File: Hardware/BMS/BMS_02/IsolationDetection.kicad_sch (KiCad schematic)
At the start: 11 parts, among them U23 OPA320-Q1

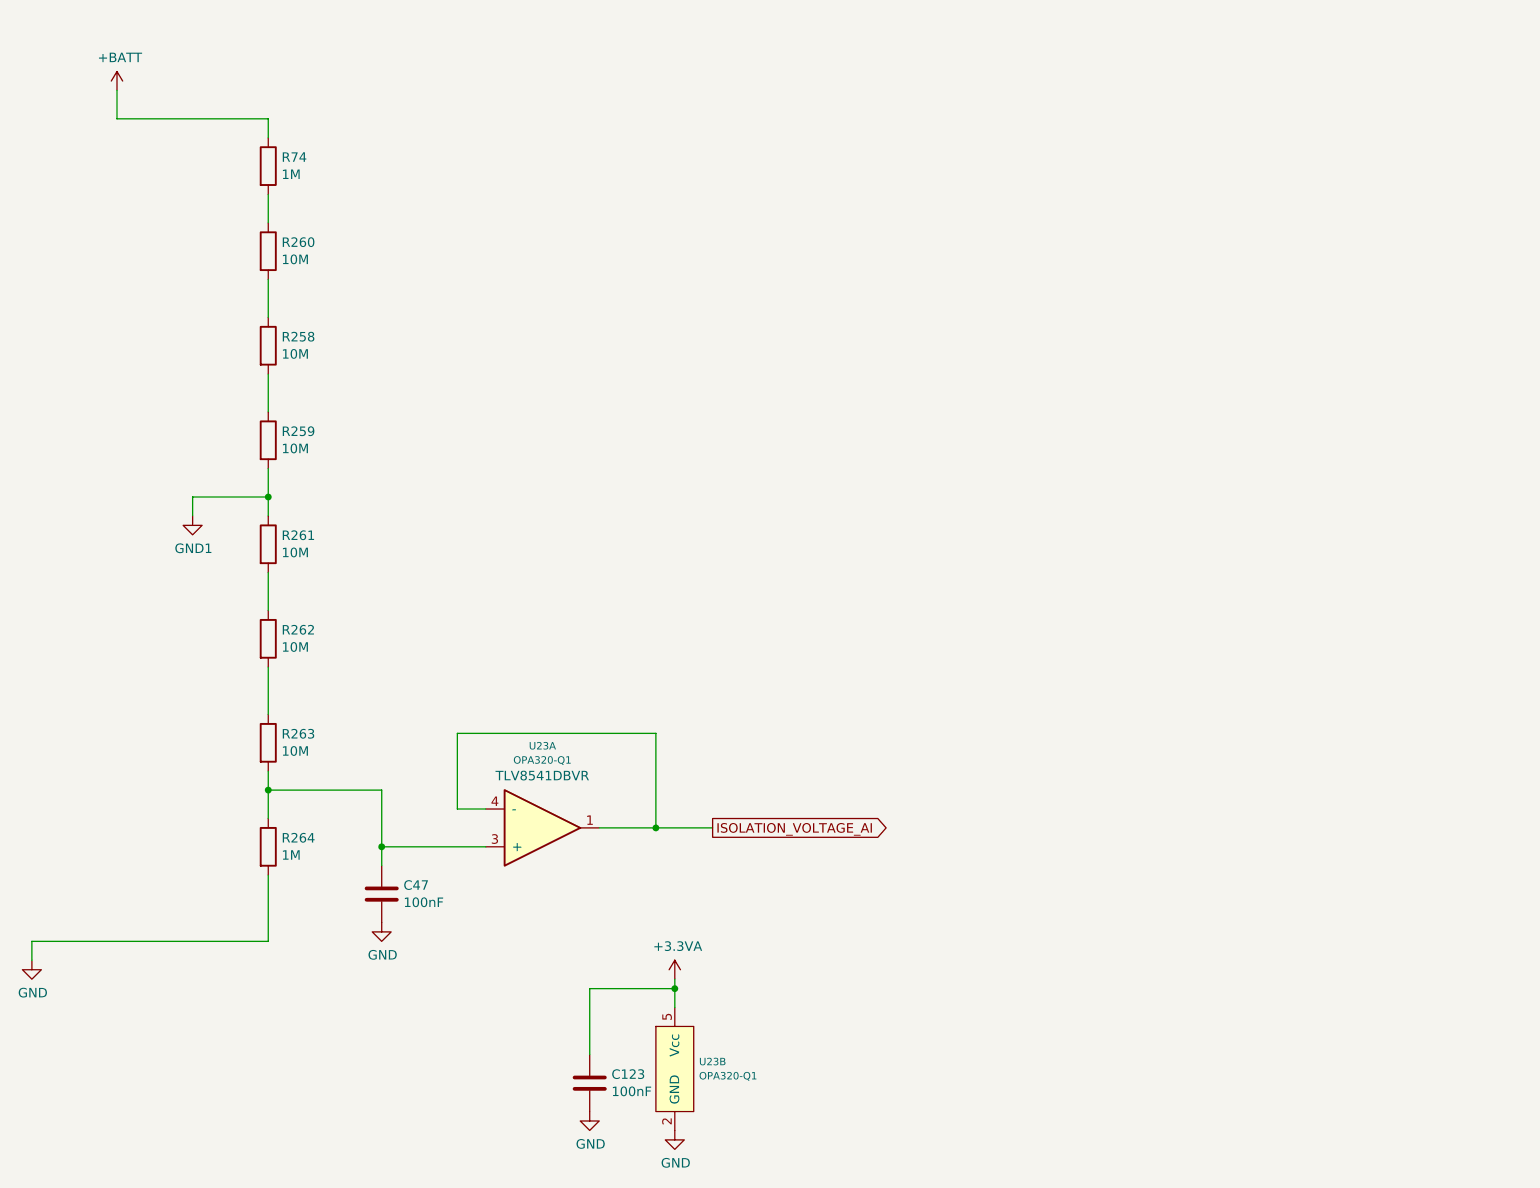
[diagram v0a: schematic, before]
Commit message: bms 02 build and code bring up. Board is built, bootloader is stable and uploads app flawlessly.
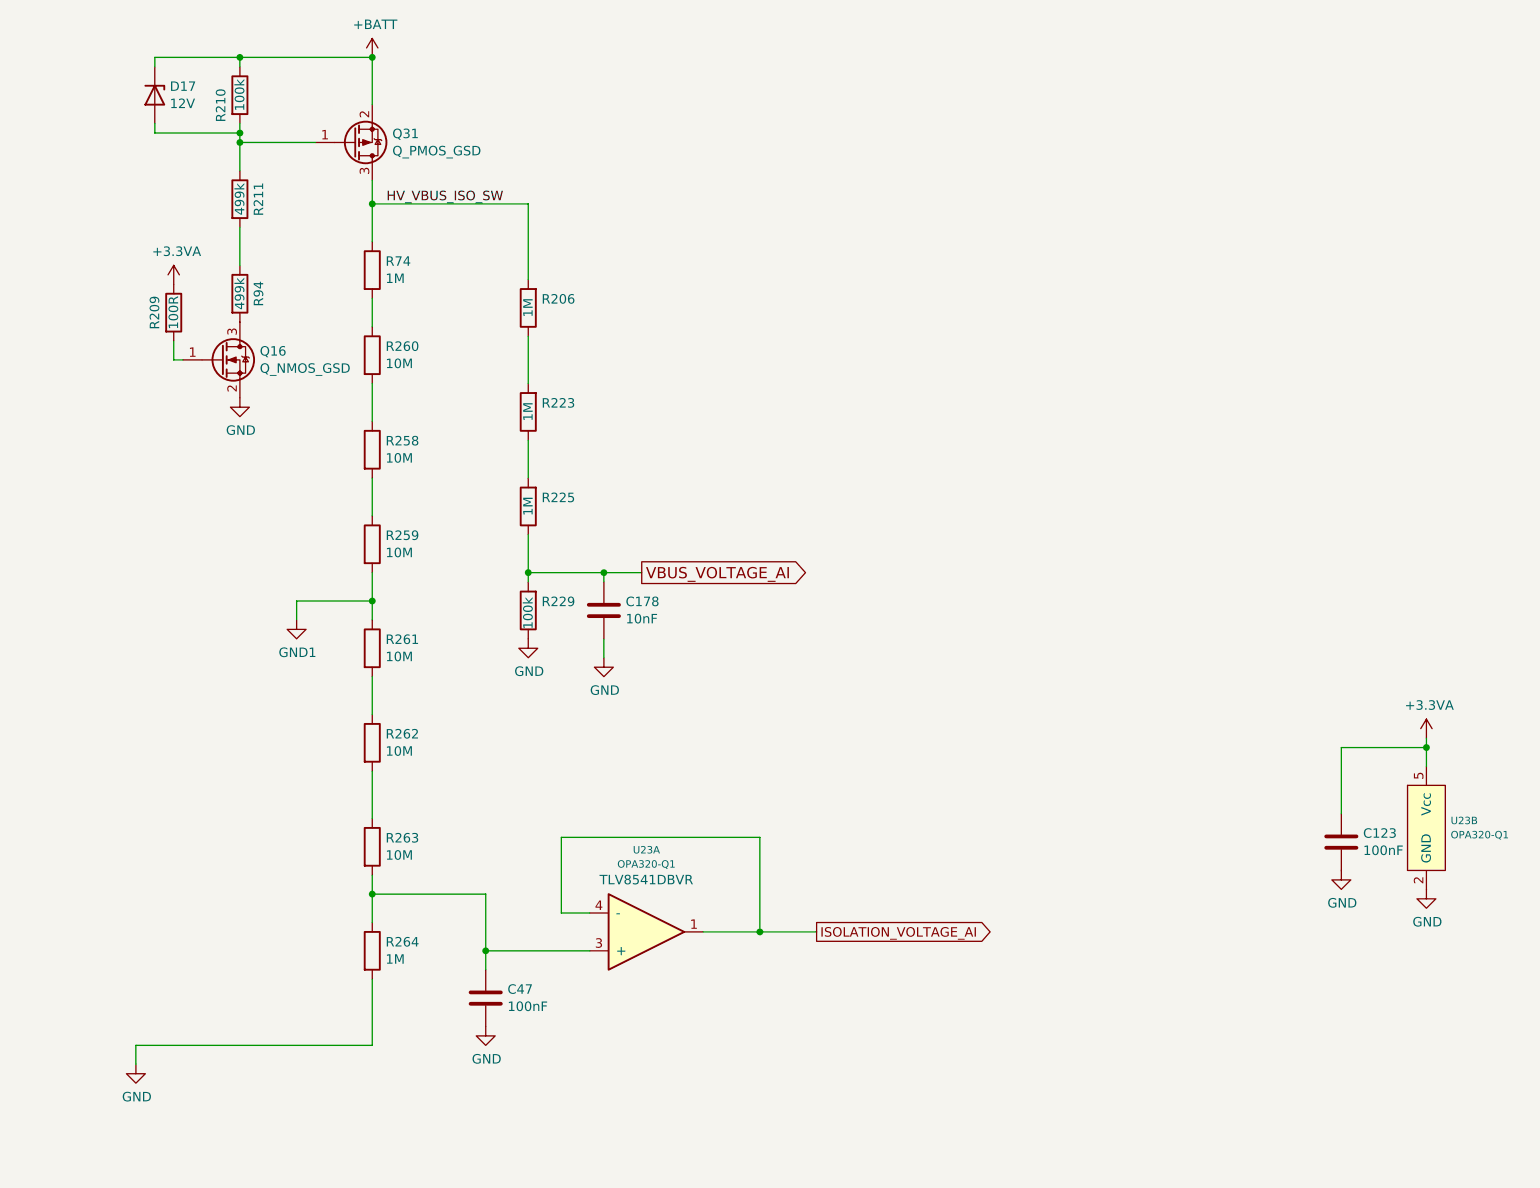
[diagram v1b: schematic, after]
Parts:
- added C178: 10nF, Capacitor_SMD:C_0603_1608Metric, symbol Device:C
- added D17: 12V, Diode_SMD:D_SOD-323F, symbol Device:D_Zener
- added Q16: Q_NMOS_GSD, Package_TO_SOT_SMD:SOT-23, symbol Device:Q_NMOS_GSD
- added Q31: Q_PMOS_GSD, Package_TO_SOT_SMD:SOT-23, symbol Device:Q_PMOS_GSD
- added R206, R223, R225: 1M, Resistor_SMD:R_0603_1608Metric, symbol Device:R
- added R209: 100R, Resistor_SMD:R_0603_1608Metric, symbol Device:R
- added R210, R229: 100k, Resistor_SMD:R_0603_1608Metric, symbol Device:R
- added R211, R94: 499k, Resistor_SMD:R_0603_1608Metric, symbol Device:R
- C123, C47: DNP < ... > -> (none)
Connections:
- net +3.3VA: now also R209.1
- net +BATT: now also D17.1 (K), Q31.2 (S), R210.1; no longer R74.1
- net GND: now also C178.2, Q16.2 (S), R229.1
- new net: R223.1, R225.2
- new net: R206.1, R223.2
- new net: D17.2 (A), Q31.1 (G), R210.2, R211.1
- new net: R211.2, R94.1
- new net: Q16.1 (G), R209.2
- new net: Q16.3 (D), R94.2
- new net HV_VBUS_ISO_SW: Q31.3 (D), R206.2, R74.1
- new net VBUS_VOLTAGE_AI: C178.1, R225.1, R229.2
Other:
- moved on the sheet: C123, C47, R258, R259, R260, R261, R262, R263, R264, R74, U23A, U23B
